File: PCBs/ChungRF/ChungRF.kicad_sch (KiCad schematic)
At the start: 9 parts, among them J1 JST-SM04B-SRSS, J2 Conn_Coaxial, U1 KB2040, U2 E22-900M30S

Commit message: ChungRF R3
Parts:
- added J3: uFL, Connector_Coaxial:U.FL_Hirose_U.FL-R-SMT-1_Vertical, symbol Connector:Conn_Coaxial
- added R1, R2: 5.1k, Capacitor_SMD:C_0603_1608Metric, symbol Device:R
- added U3: ZOE-M8Q, RF_GPS:ublox_ZOE_M8, symbol RF_GPS:ZOE-M8Q
- H1, H2: value 2.7mm_M2.5_Pad_Via -> 2.7mm_M2.5_Pad; footprint MountingHole:MountingHole_2.7mm_M2.5_Pad_Via -> besser_footprints:M2.5_2.7mm_hole
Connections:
- net GND: now also J3.2 (Ext), U3.A1 (GND), U3.A3 (GND), U3.A5 (GND), U3.A7 (GND), U3.A8 (GND), U3.A9 (GND), U3.B9 (GND), U3.C7 (GND), U3.C9 (GND), U3.D6 (GND), U3.D9 (GND), U3.E7 (GND), U3.F7 (GND), U3.G3 (GND), U3.G6 (GND), U3.G7 (GND), U3.J3 (GND), U3.J7 (RTC_I), U3.J9 (GND)
- net GNSS_SCL: now reaches U1.10 (D6)
- net GNSS_SCL: now also R1.2, U3.B1 (SCL/SPI_CLK)
- net GNSS_SDA: now reaches U1.14 (D10)
- net GNSS_SDA: now also R2.1, U3.A2 (SDA/~{SPI_CS})
- net +3V3: now reaches U1.22 (3v3)
- net +3V3: now also R1.1, R2.2, U3.G1 (V_CORE), U3.H1 (V_DCDC_OUT), U3.J1 (VCC), U3.J2 (VCC)
- new net RF_GNSS: J3.1 (In), U3.A4 (RF_IN)
- no-connect marks 12 -> 27
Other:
- note added: "GNSS Receiver (Optional)"
- note added: "Having the antenna next to the ChungRF transmitter is not ideal, but it should be fine as they are very different frequencies."
- note added: "Pin layout is bad for routing, but it works. Cannot use software SPI with radio library. Do NOT change them."
- note added: "Pull-ups may not be required per ZOE-M8Q datasheet."
- note removed: "Pin layout is bad for routing, but it works. Do NOT change them."
- moved on the sheet: U1

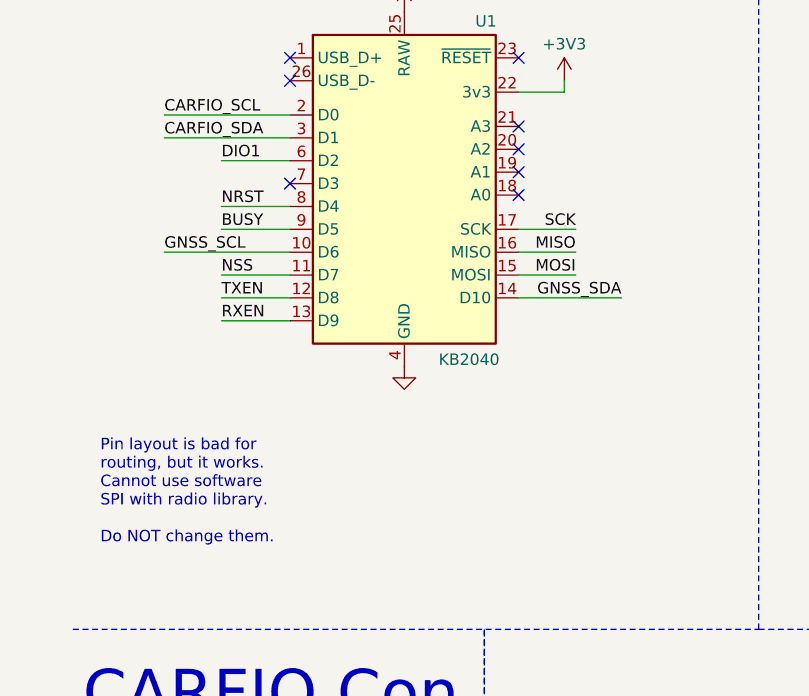
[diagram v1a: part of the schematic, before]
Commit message: ChungRF R4 - Fix GNSS I2C bus
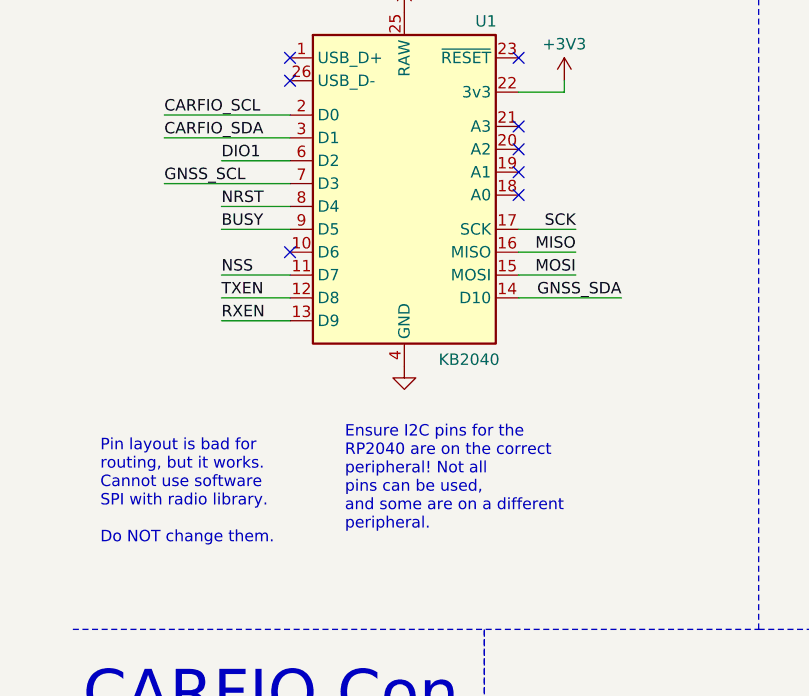
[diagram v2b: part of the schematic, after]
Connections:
- net GNSS_SCL: now also U1.7 (D3); no longer U1.10 (D6)
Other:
- note added: "Ensure I2C pins for the RP2040 are on the correct peripheral! Not all pins can be used, and some are on a different peripheral."
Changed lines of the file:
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@@
 	(title_block
 		(title "ChungRF")
-		(date "2024-11-06")
-		(rev "R3")
+		(date "2024-11-13")
+		(rev "R4")
 		(company "Chungus Aerospace")
 	)
@@
 	)
 	(no_connect
-		(at 36.83 46.99)
-	)
-	(no_connect
 		(at 205.74 49.53)
 	)
@@
 	)
 	(no_connect
+		(at 36.83 54.61)
+	)
+	(no_connect
 		(at 62.23 48.26)
 	)
@@
 	(wire
 		(pts
+			(xy 22.86 46.99) (xy 36.83 46.99)
+		)
+		(stroke
+			(width 0)
+			(type default)
+		)
+	)
+	(wire
+		(pts
 			(xy 29.21 49.53) (xy 36.83 49.53)
 		)
@@
 	(wire
 		(pts
-			(xy 22.86 54.61) (xy 36.83 54.61)
-		)
-		(stroke
-			(width 0)
-			(type default)
-		)
-	)
-	(wire
-		(pts
 			(xy 107.95 72.39) (xy 115.57 72.39)
 		)
@@
 		(exclude_from_sim no)
 		(at 158.75 58.42 0)
+		(effects
+			(font
+				(size 1.27 1.27)
+			)
+			(justify left)
+		)
+	)
+	(text "Ensure I2C pins for the \nRP2040 are on the correct\nperipheral! Not all \npins can be used,\nand some are on a different\nperipheral."
+		(exclude_from_sim no)
+		(at 42.926 79.756 0)
 		(effects
 			(font
@@
 	)
 	(label "GNSS_SCL"
-		(at 22.86 54.61 0)
+		(at 22.86 46.99 0)
 		(fields_autoplaced yes)
 		(effects
